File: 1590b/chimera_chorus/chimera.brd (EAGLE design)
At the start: 49.5 x 61 mm, 42 parts, among them IC1 TL072, IC2 TL072, IC3 MN3007, IC4 CD4046

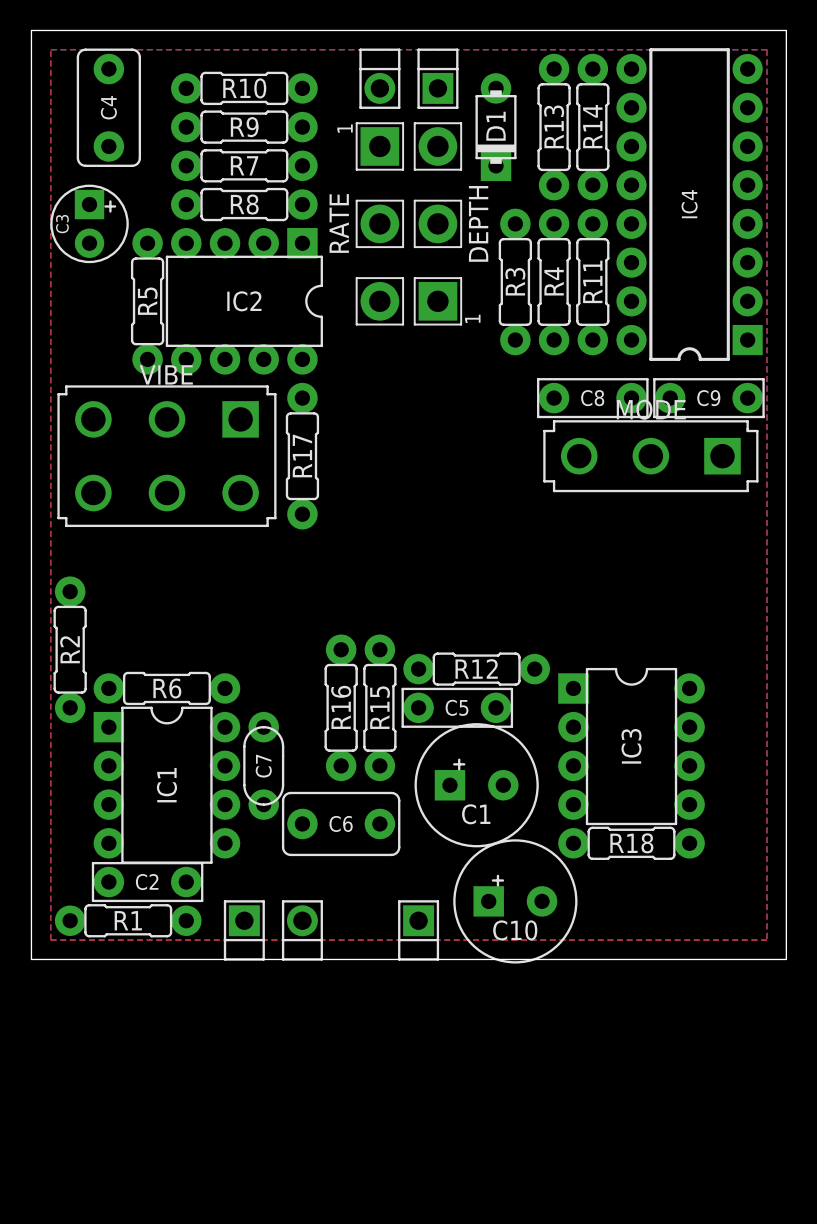
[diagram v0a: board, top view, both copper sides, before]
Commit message: prettified schematics a bit
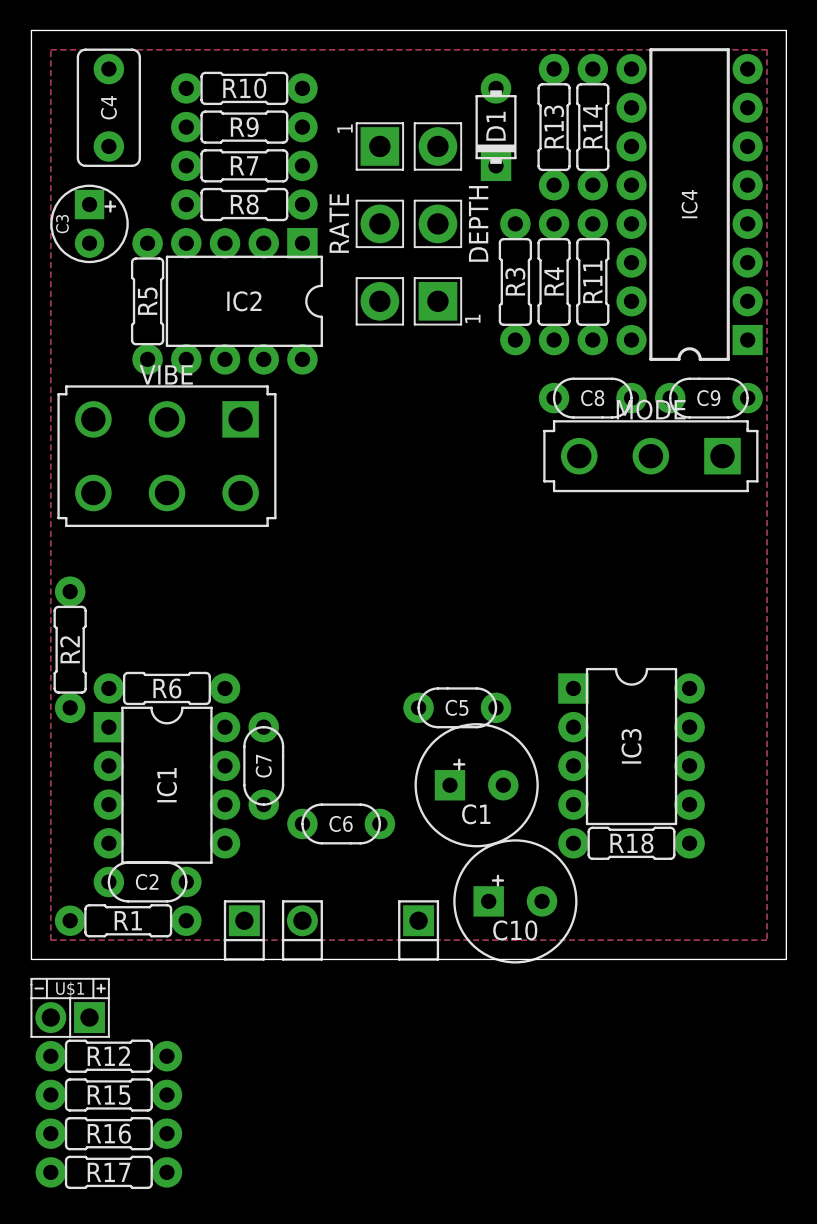
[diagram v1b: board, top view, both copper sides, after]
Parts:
- removed PAD3: PADSQR, supply pins:SQUARE
- removed PAD5: PADRND, supply pins:ROUND
- added U$1: DC_MONO, jacks:DC
- C1: value 470uF -> 470u
- C2, C5, C8, C9: device capacitors-film:BOX_SMALL -> capacitors-film:050X030_025_2
- C3: value 10uF -> 10u
- C6: device capacitors-film:BOX_MED -> capacitors-film:050X030_025_2
- moved R17 48.7 mm to (5.08, -14.0), turned to 0 degrees
- moved R12 35.0 mm to (5.08, -6.35)
- moved R16 31.8 mm to (5.08, -11.4), turned to 0 degrees
- moved R15 31.0 mm to (5.08, -8.89), turned to 0 degrees
- renumbered PAD1 to IN, PAD2 to OUT, PAD4 to GND
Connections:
- removed net +9V: D1.A, PAD3.1
- removed net N$25: R17.1, VIBE.B1
- removed net VA: C1.+, D1.C, IC1.8, IC2.8, IC3.1, IC4.14, IC4.16, R11.2, R4.2
- new net N$26: C3.+, IC2.2, R2.1, R3.2, R4.2, R5.1, R7.1
- new net N$29: D1.A, U$1.T
- new net VC: C1.+, D1.C, IC1.8, IC2.8, IC3.1, IC4.14, IC4.16, R11.1, R4.1
- net GND: now also U$1.S; no longer PAD5.1
- net N$10: now also DEPTH.3, IC2.7, R9.2; no longer IC2.5, R10.2
- net N$16: now also R11.2, R12.1; no longer R11.1, R12.2
- net N$17: now also R16.2; no longer R16.1
- net N$18: now also R12.2, R15.1; no longer R12.1, R15.2
- net N$19: now also R15.2, R16.1; no longer R15.1, R16.2
- net N$23: now also VIBE.B1; no longer VIBE.A1
- net N$5: now also IC2.5, R10.2; no longer DEPTH.3, IC2.7, R9.1
- net N$6: now also R17.1, VIBE.A1; no longer C3.+, IC2.2, R2.1, R3.2, R4.1, R5.1, R7.1
- net N$7: now also R8.1, R9.1; no longer R8.2, R9.2
- net N$8: now also R8.2; no longer R8.1
